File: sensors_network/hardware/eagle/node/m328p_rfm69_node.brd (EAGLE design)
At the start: 65.5 x 39.9 mm, 32 parts, among them IC2 L6920, U1 M328P, U2 RFM69W, Y1 8MHz

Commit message: [sensors network] small pcb/schematic final touches
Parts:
- moved C6 2.05 mm to (52.6, 35.1)
- moved C8 2.05 mm to (7.11, 22.6)
- moved JP3 2.05 mm to (19.1, 31.0)
- moved L1 2.05 mm to (7.11, 16.3)
- moved CT1 2.05 mm to (62.0, 20.3)
- moved IC2 2.05 mm to (13.7, 18.5)
- moved R2 2.05 mm to (50.8, 20.3)
- moved RB2 2.05 mm to (53.8, 22.4)
- moved SJ2 2.05 mm to (19.3, 21.8)
- moved Y1 2.05 mm to (37.6, 17.0)
- moved JP1 2.05 mm to (9.91, 37.3)
- moved SJ1 2.05 mm to (10.4, 27.4)
- moved BAT4 2.05 mm to (31.5, 9.40)
- moved C10 2.05 mm to (39.9, 13.0)
- moved C11 2.05 mm to (13.7, 13.2)
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
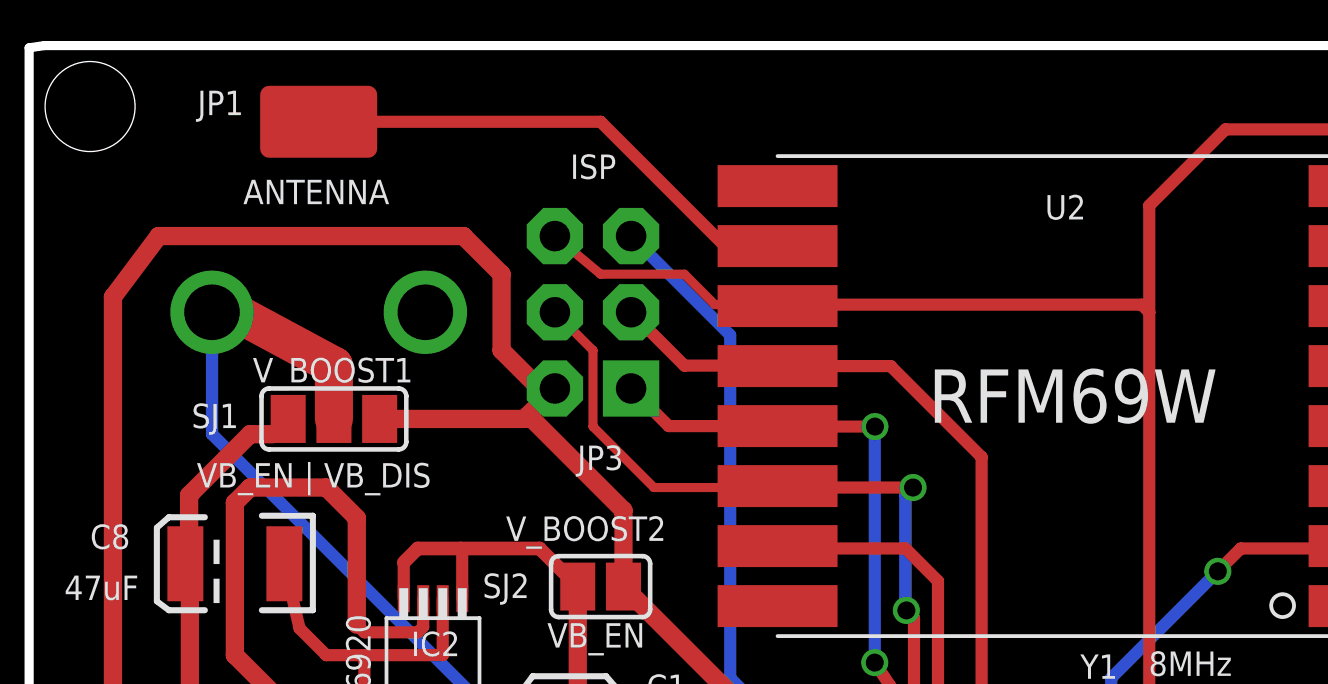
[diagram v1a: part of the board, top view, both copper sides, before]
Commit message: [sensors network] added missing ground connection for RFM69 module
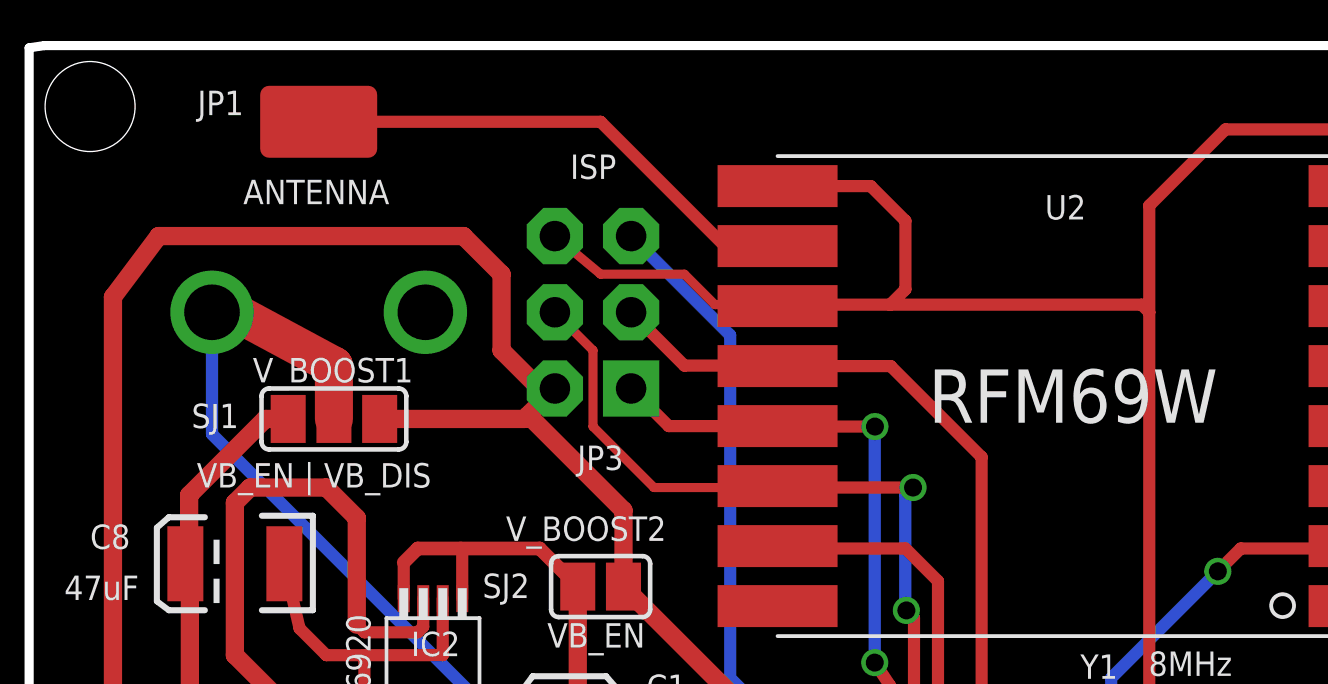
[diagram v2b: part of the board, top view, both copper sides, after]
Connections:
- net GND: now also U2.9
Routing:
- net GND: track 210.2 -> 218.0 mm
- net N$2: track 13.6 -> 14.4 mm
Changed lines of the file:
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@@
 <wire x1="19.304" y1="32.258" x2="17.78" y2="33.528" width="0.3048" layer="1"/>
 <wire x1="25.25" y1="31.242" x2="25.202" y2="31.194" width="0.4064" layer="1"/>
-<wire x1="25.25" y1="31.242" x2="37.338" y2="31.242" width="0.4064" layer="1"/>
+<wire x1="25.25" y1="31.242" x2="28.956" y2="31.242" width="0.4064" layer="1"/>
+<wire x1="28.956" y1="31.242" x2="37.338" y2="31.242" width="0.4064" layer="1"/>
 <wire x1="37.338" y1="31.242" x2="37.592" y2="30.988" width="0.4064" layer="1"/>
 <wire x1="14.041" y1="21.442" x2="14.041" y2="19.558" width="0.4064" layer="1"/>
@@
 <wire x1="63.5" y1="11.684" x2="59.182" y2="11.684" width="0.4064" layer="1"/>
 <wire x1="59.182" y1="11.684" x2="57.912" y2="12.954" width="0.4064" layer="1"/>
+<contactref element="U2" pad="9"/>
+<wire x1="25.202" y1="35.194" x2="28.306" y2="35.194" width="0.4064" layer="1"/>
+<wire x1="28.306" y1="35.194" x2="29.464" y2="34.036" width="0.4064" layer="1"/>
+<wire x1="29.464" y1="34.036" x2="29.464" y2="31.75" width="0.4064" layer="1"/>
+<wire x1="29.464" y1="31.75" x2="28.956" y2="31.242" width="0.4064" layer="1"/>
 </signal>
 <signal name="MOSI">
@@
 <wire x1="5.588" y1="24.892" x2="5.588" y2="22.732" width="0.6096" layer="1"/>
 <wire x1="5.588" y1="22.732" x2="5.462" y2="22.606" width="0.6096" layer="1"/>
-<wire x1="8.382" y1="26.924" x2="7.62" y2="26.924" width="0.6096" layer="1"/>
-<wire x1="7.62" y1="26.924" x2="5.588" y2="24.892" width="0.6096" layer="1"/>
-<wire x1="8.382" y1="26.924" x2="8.89" y2="27.432" width="0" layer="19" extent="1-1"/>
+<wire x1="8.128" y1="27.432" x2="5.588" y2="24.892" width="0.6096" layer="1"/>
+<wire x1="8.89" y1="27.432" x2="8.128" y2="27.432" width="0.6096" layer="1"/>
 </signal>
 <signal name="N$7">
